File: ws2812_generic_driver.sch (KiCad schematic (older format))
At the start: 14 parts, among them J1 Conn_01x01, J2 Conn_01x01, J3 Conn_ARM_JTAG_SWD_10, J4 Conn_01x01, J5 Conn_01x01, J6 Conn_01x01, J7 Conn_01x01, U1 ATSAMD21E15L-A, U2 TC2014-3.3VxCTTR

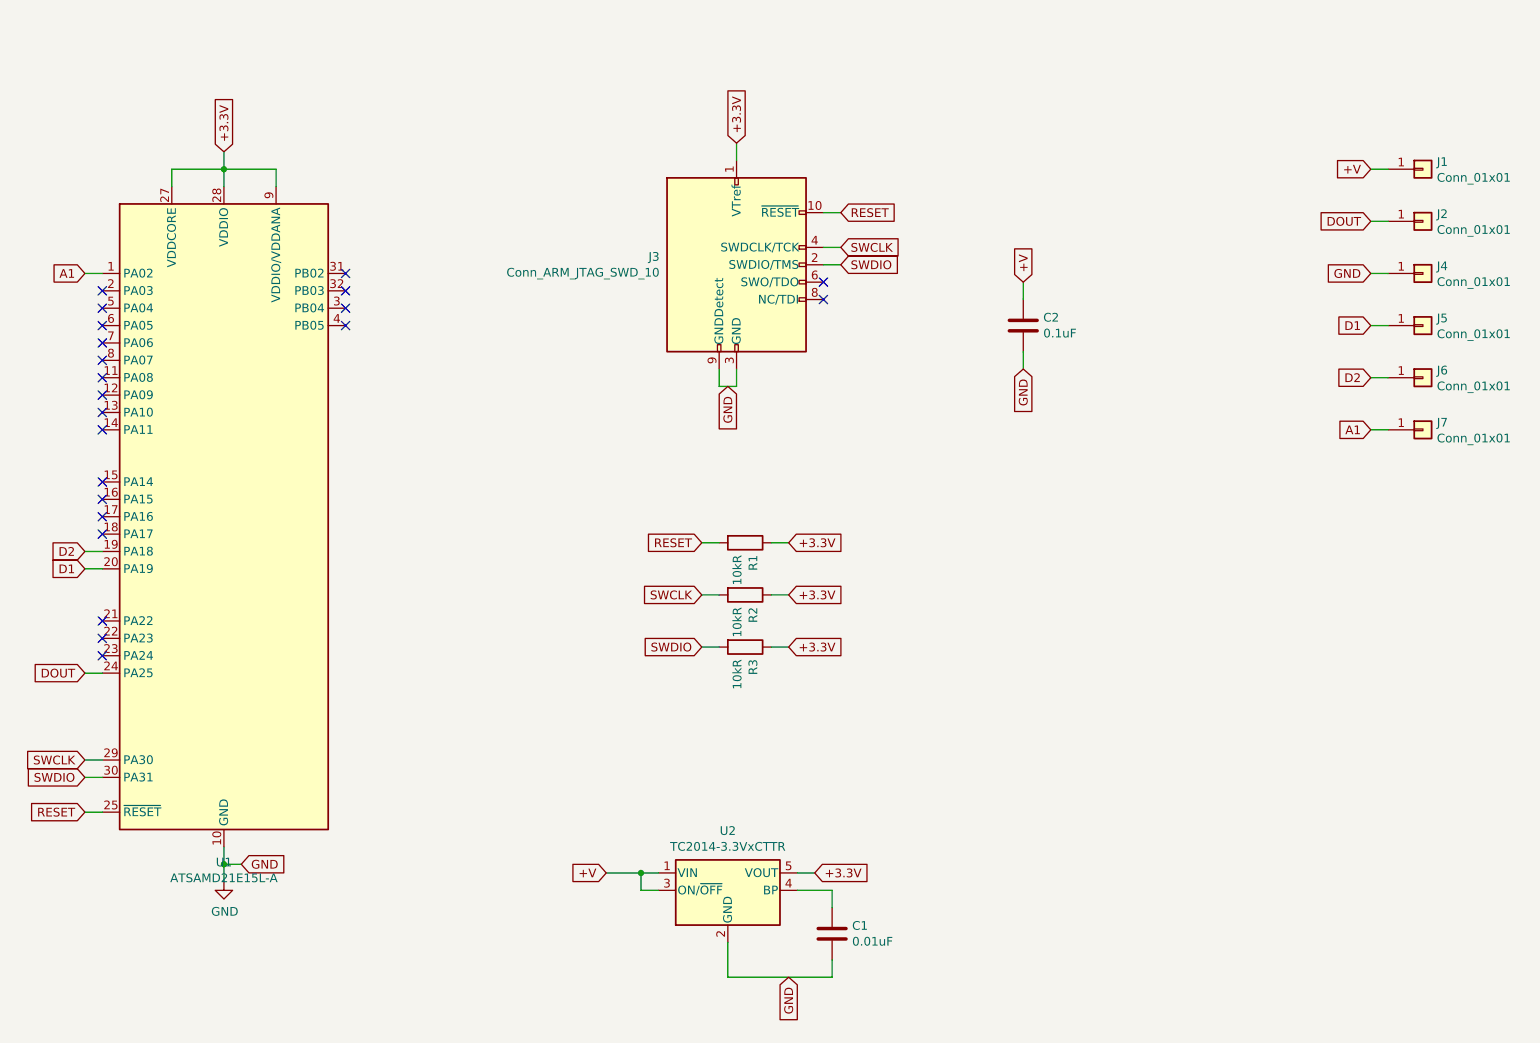
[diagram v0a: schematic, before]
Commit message: Add attiny10 hardware spi->ws2812 support
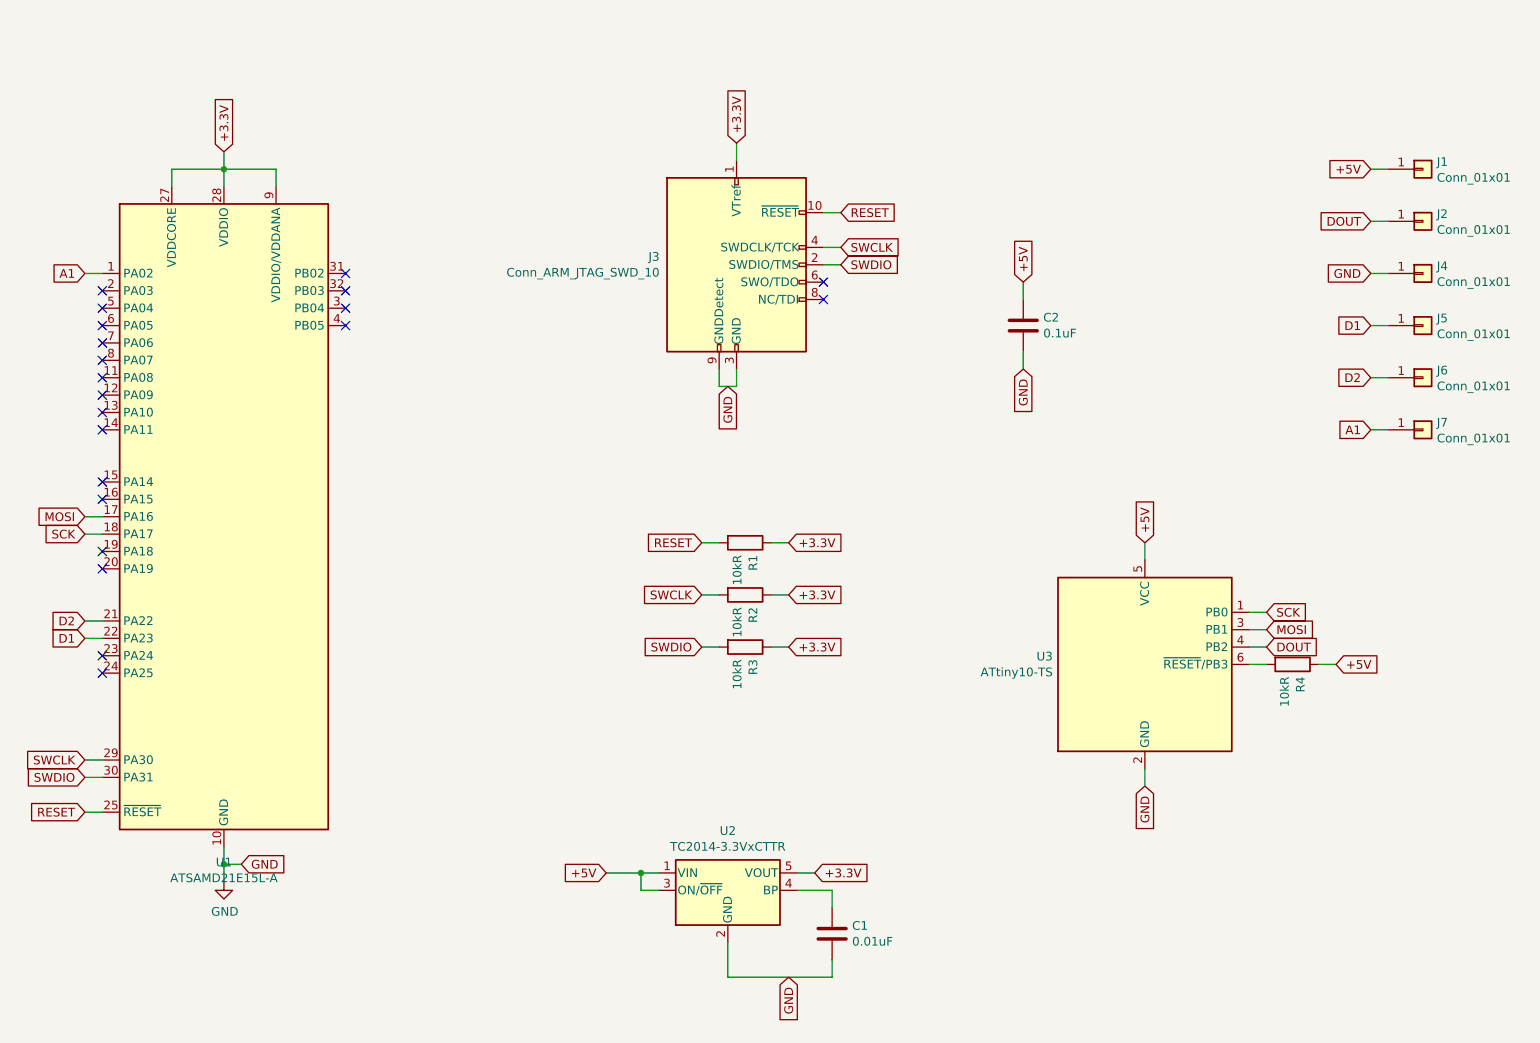
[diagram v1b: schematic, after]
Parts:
- added R4: 10kR, Resistor_SMD:R_0805_2012Metric, symbol Device:R
- added U3: ATtiny10-TS, Package_TO_SOT_SMD:SOT-23-6, symbol MCU_Microchip_ATtiny:ATtiny10-TS
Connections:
- net D1: now also U1.22 (PA23); no longer U1.20 (PA19)
- net D2: now also U1.21 (PA22); no longer U1.19 (PA18)
- net DOUT: now also U3.4 (PB2); no longer U1.24 (PA25)
- net GND: now also U3.2 (GND)
- net MOSI: now reaches U1.17 (PA16)
- net MOSI: now also U3.3 (PB1)
- net SCK: now reaches U1.18 (PA17)
- net SCK: now also U3.1 (PB0)
- net +V renamed +5V
- net +5V: now also R4.1, U3.5 (VCC)
- new net: R4.2, U3.6 (~RESET~/PB3)
- no-connect marks 22 -> 21
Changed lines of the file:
@@
 $EndComp
 Text GLabel 5100 5550 0    50   Input ~ 0
-+V
++5V
 Text GLabel 6300 5550 2    50   Input ~ 0
 +3.3V
@@
 	6200 5550 6300 5550
 Text GLabel 9500 1500 0    50   Input ~ 0
-+V
++5V
 Text GLabel 9500 2100 0    50   Input ~ 0
 GND
@@
 Text GLabel 9500 3000 0    50   Input ~ 0
 A1
-Text GLabel 2100 4400 0    50   Input ~ 0
+Text GLabel 8900 4250 2    50   Input ~ 0
 DOUT
 Wire Wire Line
-	2100 4400 2200 4400
-Text GLabel 2100 3800 0    50   Input ~ 0
+	8900 4250 8800 4250
+Text GLabel 2100 4200 0    50   Input ~ 0
 D1
-Text GLabel 2100 3700 0    50   Input ~ 0
+Text GLabel 2100 4100 0    50   Input ~ 0
 D2
 Text GLabel 2100 2100 0    50   Input ~ 0
@@
 	2200 2100 2100 2100
 Wire Wire Line
-	2200 3700 2100 3700
-Wire Wire Line
-	2100 3800 2200 3800
+	2200 4100 2100 4100
+Wire Wire Line
+	2100 4200 2200 4200
 NoConn ~ 3600 2100
 NoConn ~ 3600 2200
@@
 NoConn ~ 2200 3300
 NoConn ~ 2200 3400
-NoConn ~ 2200 3500
-NoConn ~ 2200 3600
-NoConn ~ 2200 4100
-NoConn ~ 2200 4200
+NoConn ~ 2200 3700
+NoConn ~ 2200 3800
 NoConn ~ 2200 4300
 $Comp
@@
 $EndComp
 Text GLabel 7500 2150 1    50   Input ~ 0
-+V
++5V
 Wire Wire Line
 	7500 2150 7500 2250
@@
 Wire Wire Line
 	7500 2650 7500 2550
+$Comp
+L MCU_Microchip_ATtiny:ATtiny10-TS U3
+U 1 1 5FAF4A70
+P 8200 4350
+F 0 "U3" H 7670 4396 50  0000 R CNN
+F 1 "ATtiny10-TS" H 7670 4305 50  0000 R CNN
+F 2 "Package_TO_SOT_SMD:SOT-23-6" H 8200 4350 50  0001 C CIN
+F 3 "http://ww1.microchip.com/downloads/en/DeviceDoc/Atmel-8127-AVR-8-bit-Microcontroller-ATtiny4-ATtiny5-ATtiny9-ATtiny10_Datasheet.pdf" H 8200 4350 50  0001 C CNN
+	1    8200 4350
+	1    0    0    -1
+$EndComp
+Text GLabel 8200 3650 1    50   Input ~ 0
++5V
+Wire Wire Line
+	8200 3650 8200 3750
+Text GLabel 8200 5050 3    50   Input ~ 0
+GND
+Wire Wire Line
+	8200 5050 8200 4950
+$Comp
+L Device:R R4
+U 1 1 5FAF8F9F
+P 9050 4350
+F 0 "R4" H 9120 4396 50  0000 L CNN
+F 1 "10kR" H 9120 4305 50  0000 L CNN
+F 2 "Resistor_SMD:R_0805_2012Metric" V 8980 4350 50  0001 C CNN
+F 3 "~" H 9050 4350 50  0001 C CNN
+	1    9050 4350
+	0    1    1    0
+$EndComp
+Text GLabel 9300 4350 2    50   Input ~ 0
++5V
+Wire Wire Line
+	9300 4350 9200 4350
+Wire Wire Line
+	8900 4350 8800 4350
+NoConn ~ 2200 4400
+Text GLabel 2100 3500 0    50   Input ~ 0
+MOSI
+Text GLabel 2100 3600 0    50   Input ~ 0
+SCK
+Wire Wire Line
+	2200 3500 2100 3500
+Wire Wire Line
+	2100 3600 2200 3600
+Text GLabel 8900 4150 2    50   Input ~ 0
+MOSI
+Text GLabel 8900 4050 2    50   Input ~ 0
+SCK
+Wire Wire Line
+	8800 4150 8900 4150
+Wire Wire Line
+	8900 4050 8800 4050
 $EndSCHEMATC

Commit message: Fix core overvoltage problem
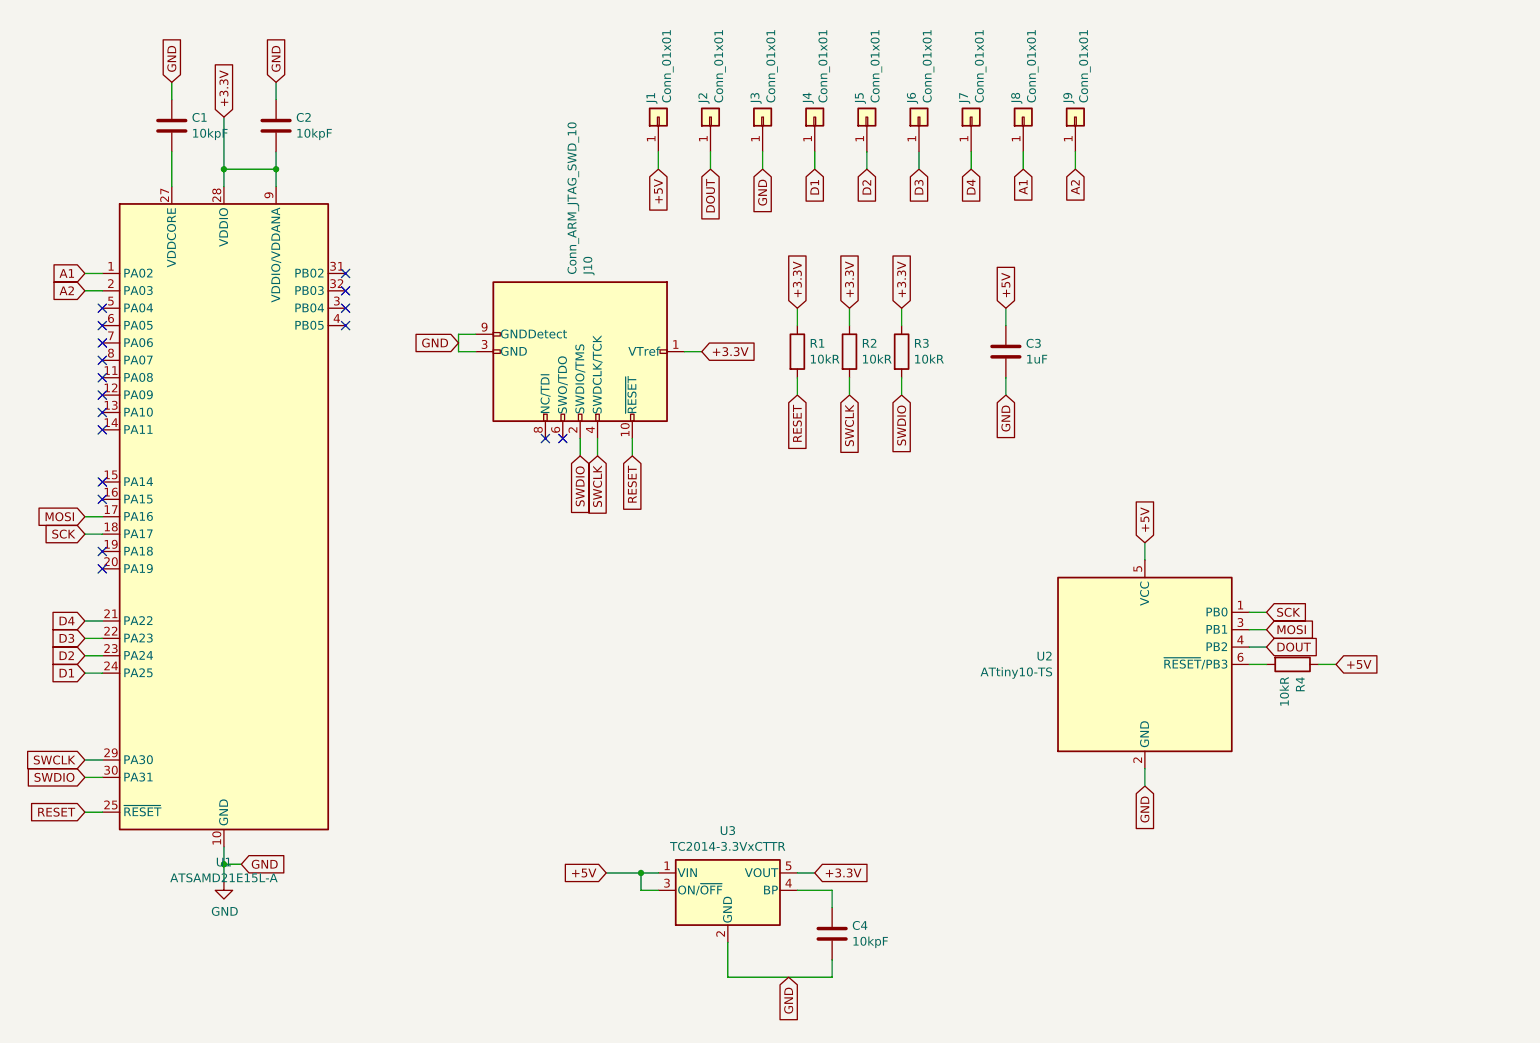
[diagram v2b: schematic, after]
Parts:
- added C1, C2: 10kpF, Capacitor_SMD:C_0603_1608Metric, symbol Device:C
- added J6, J7, J9: Conn_01x01, TestPoint:TestPoint_Pad_1.5x1.5mm, symbol Connector_Generic:Conn_01x01
- C3: renamed from C2; value 0.1uF -> 1uF; footprint Capacitor_SMD:C_0603_1608Metric -> Capacitor_SMD:C_0805_2012Metric
- C4: renamed from C1; value 0.01uF -> 10kpF
- J10: renamed from J3; footprint Connector_PinHeader_1.00mm:PinHeader_2x05_P1.00mm_Vertical -> Connector_PinHeader_1.27mm:PinHeader_2x05_P1.27mm_Vertical
- renumbered J4 to J3, J5 to J4, J6 to J5, J7 to J8, U3 to U2, U2 to U3
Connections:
- net +3.3V: now also C2.2; no longer U1.27 (VDDCORE)
- net D1: now also U1.24 (PA25); no longer U1.22 (PA23)
- net D2: now also U1.23 (PA24); no longer U1.21 (PA22)
- net GND: now also C1.1, C2.1
- net A2: now reaches U1.2 (PA03)
- net A2: now also J9.1 (Pin_1)
- new net: C1.2, U1.27 (VDDCORE)
- new net D3: J6.1 (Pin_1), U1.22 (PA23)
- new net D4: J7.1 (Pin_1), U1.21 (PA22)
- no-connect marks 21 -> 18
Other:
- moved on the sheet: C3, J1, J10, J2, J3, J4, J5, J8, R1, R2, R3
